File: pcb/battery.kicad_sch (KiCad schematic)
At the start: 45 parts

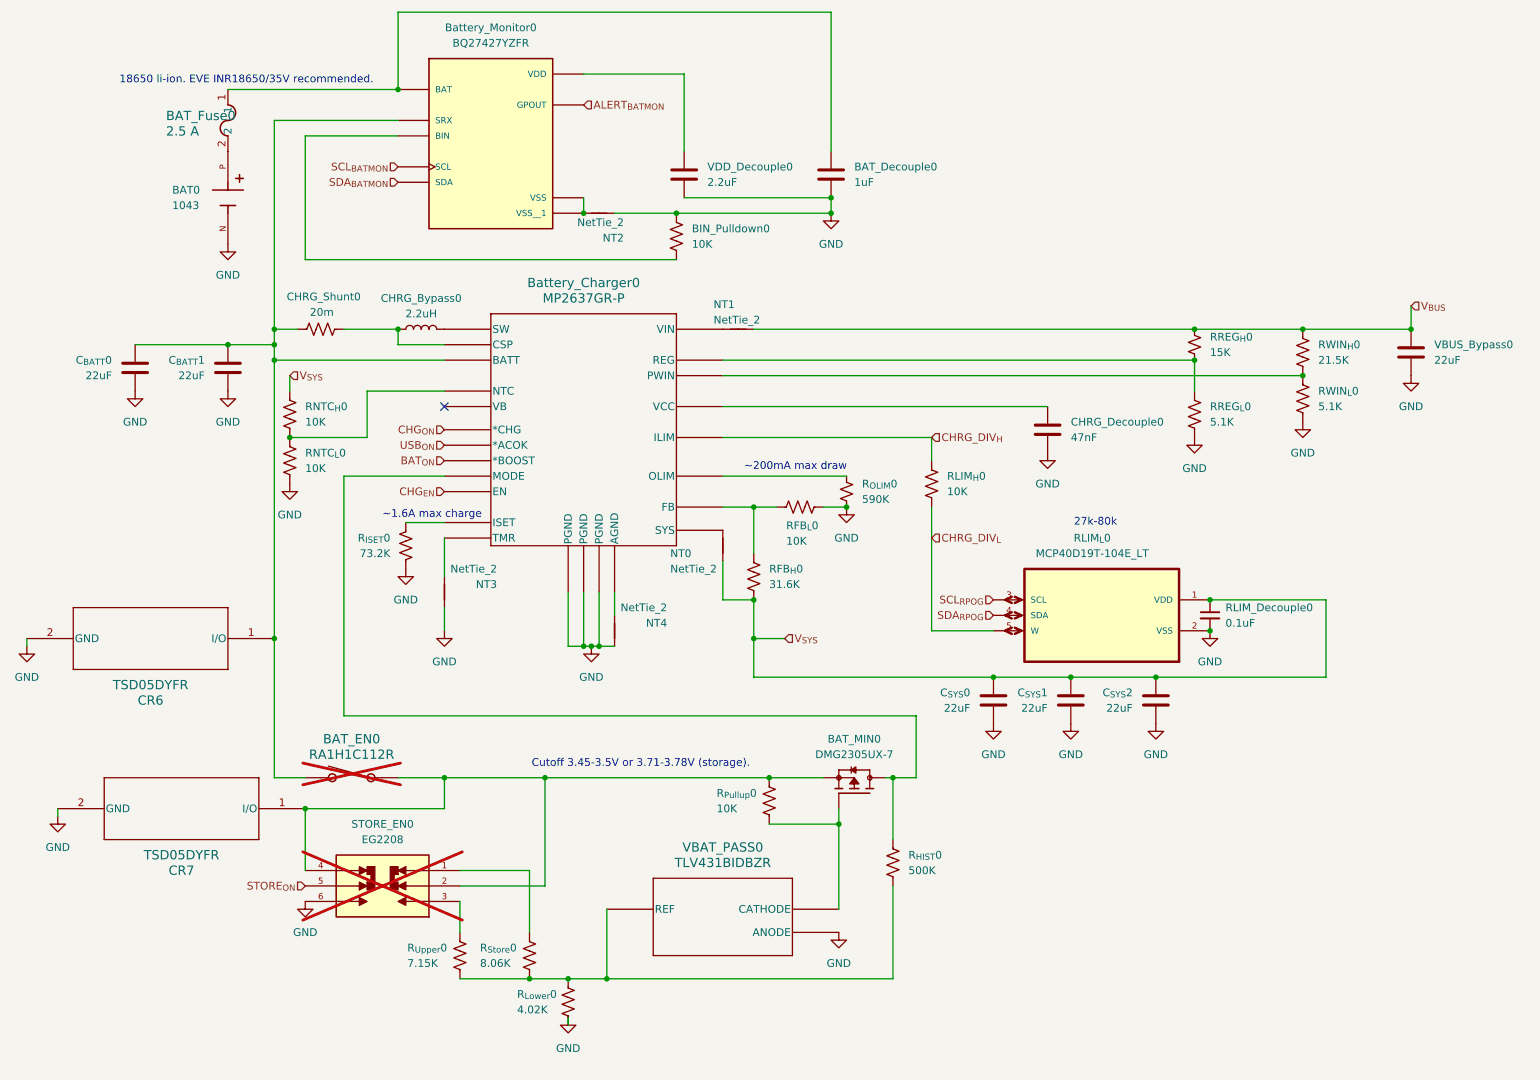
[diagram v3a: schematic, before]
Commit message: Create right hand order for JLCPCB
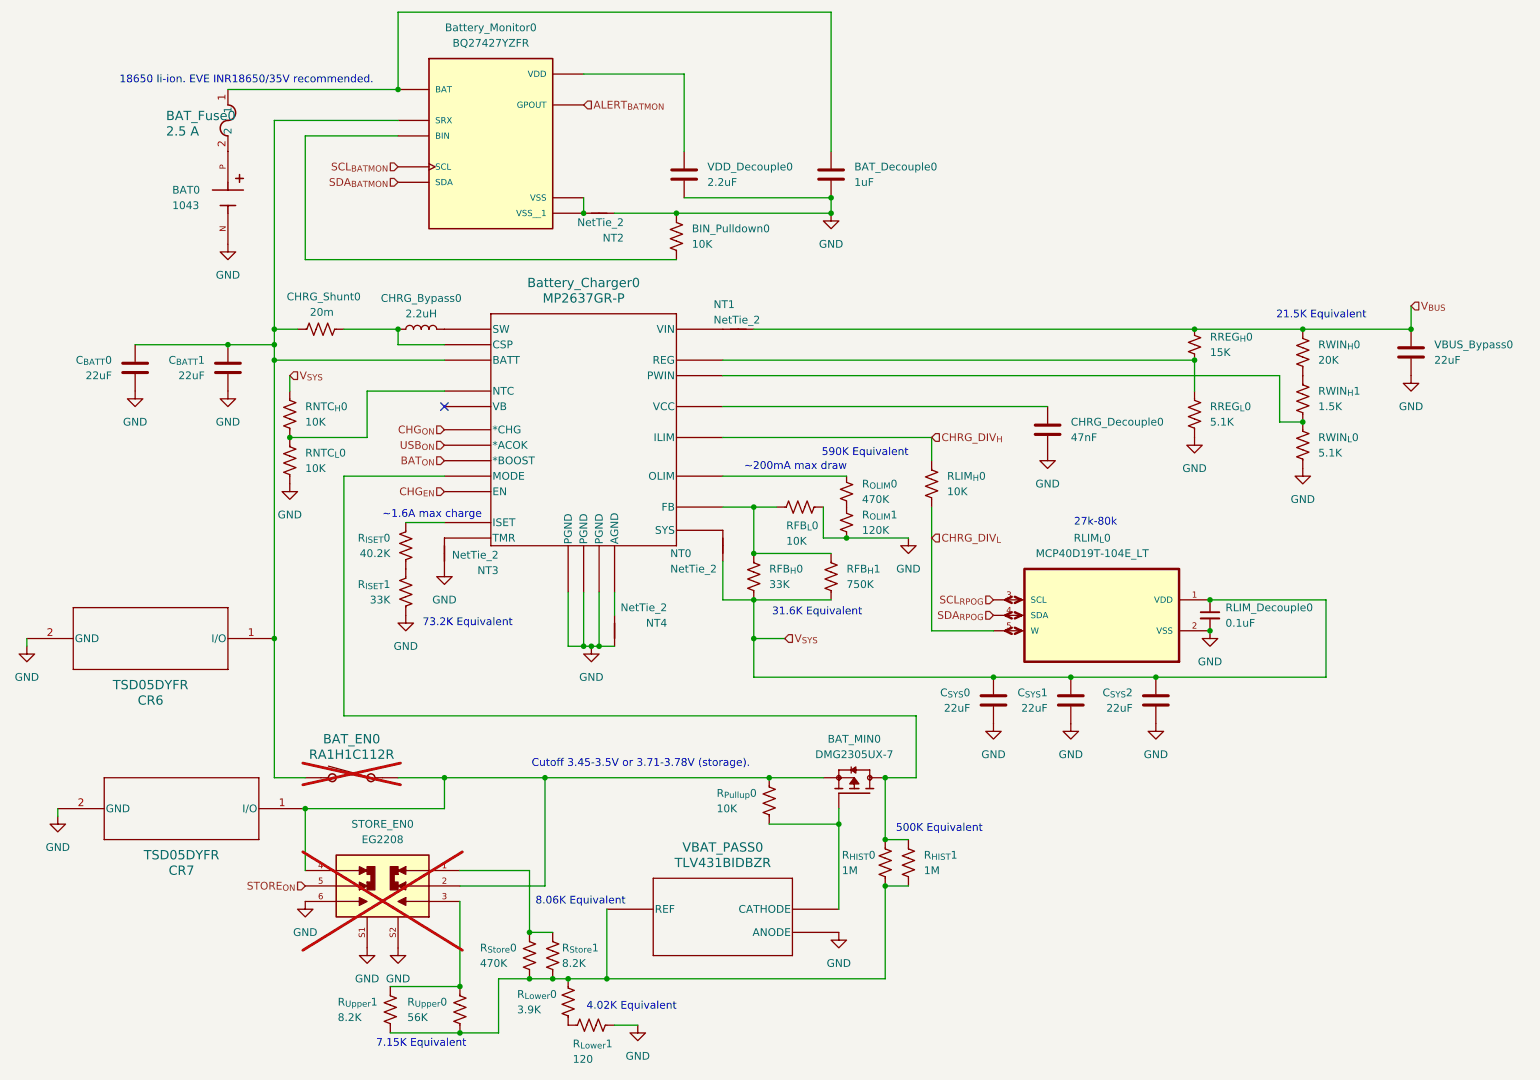
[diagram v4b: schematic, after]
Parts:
- added RFB_{H}1: 750K, Resistor_SMD:R_0603_1608Metric, symbol Device:R_US
- added RWIN_{H}1: 1.5K, Resistor_SMD:R_0402_1005Metric, symbol Device:R_US
- added R_{HIST}1: 1M, Resistor_SMD:R_0402_1005Metric, symbol Device:R_US
- added R_{ISET}1: 33K, Resistor_SMD:R_0603_1608Metric, symbol Device:R_US
- added R_{Lower}1: 120, Resistor_SMD:R_0603_1608Metric, symbol Device:R_US
- added R_{OLIM}1: 120K, Resistor_SMD:R_0402_1005Metric, symbol Device:R_Small_US
- added R_{Store}1, R_{Upper}1: 8.2K, Resistor_SMD:R_0402_1005Metric, symbol Device:R_US
- BAT_Decouple0: LCSC C2823 -> C28323
- CHRG_Bypass0: footprint Inductor_SMD:L_1210_3225Metric -> Inductor_SMD:L_0805_2012Metric; LCSC C70960 -> C1043
- C_{BATT}0, C_{BATT}1, C_{SYS}0, C_{SYS}1, C_{SYS}2, VBUS_Bypass0: LCSC C12891 -> C5672
- RFB_{H}0: value 31.6K -> 33K; footprint Resistor_SMD:R_0805_2012Metric -> Resistor_SMD:R_0603_1608Metric; LCSC C17623 -> C4216
- RWIN_{H}0: value 21.5K -> 20K; footprint Resistor_SMD:R_0805_2012Metric -> Resistor_SMD:R_0402_1005Metric; LCSC C17545 -> C25765
- R_{HIST}0: value 500K -> 1M; footprint Resistor_SMD:R_0805_2012Metric -> Resistor_SMD:R_0402_1005Metric; LCSC C3097783 -> C26083
- R_{ISET}0: value 73.2K -> 40.2K; footprint Resistor_SMD:R_0805_2012Metric -> Resistor_SMD:R_0603_1608Metric; LCSC C17814 -> C12447
- R_{Lower}0: value 4.02K -> 3.9K; footprint Resistor_SMD:R_0805_2012Metric -> Resistor_SMD:R_0603_1608Metric; LCSC C17663 -> C23018
- R_{OLIM}0: value 590K -> 470K; footprint Resistor_SMD:R_0805_2012Metric -> Resistor_SMD:R_0402_1005Metric; LCSC C17762 -> C25790
- R_{Store}0: value 8.06K -> 470K; footprint Resistor_SMD:R_0805_2012Metric -> Resistor_SMD:R_0402_1005Metric; LCSC C19006 -> C25790
- R_{Upper}0: value 7.15K -> 56K; footprint Resistor_SMD:R_0805_2012Metric -> Resistor_SMD:R_0402_1005Metric; LCSC C17806 -> C25796
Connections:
- net GND: now also STORE_EN0.S1, STORE_EN0.S2, R_{ISET}1.2, R_{Lower}1.2, R_{OLIM}1.2; no longer R_{ISET}0.2, R_{Lower}0.2, R_{OLIM}0.2
- net V_{SYS}: now also RFB_{H}1.2
- net at R_{HIST}0.2, R_{Lower}0.1, R_{Store}0.2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: now also R_{HIST}1.2, R_{Store}1.2, R_{Upper}1.2
- net at BAT_MIN0.3, Battery_Charger0.19 (MODE), R_{HIST}0.1: now also R_{HIST}1.1
- net at Battery_Charger0.14 (PWIN), RWIN_{L}0.1: now also RWIN_{H}1.2; no longer RWIN_{H}0.2
- net at Battery_Charger0.10 (FB), RFB_{H}0.1, RFB_{L}0.2: now also RFB_{H}1.1
- net at R_{Upper}0.1, STORE_EN0.3: now also R_{Upper}1.1
- net at R_{Store}0.1, STORE_EN0.1: now also R_{Store}1.1
- new net: R_{Lower}0.2, R_{Lower}1.1
- new net: R_{ISET}0.2, R_{ISET}1.1
- new net: RWIN_{H}0.2, RWIN_{H}1.1
- new net: R_{OLIM}0.2, R_{OLIM}1.1
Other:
- note added: "21.5K Equivalent"
- note added: "31.6K Equivalent"
- note added: "4.02K Equivalent"
- note added: "500K Equivalent"
- note added: "590K Equivalent"
- note added: "7.15K Equivalent"
- note added: "73.2K Equivalent"
- note added: "8.06K Equivalent"
- moved on the sheet: NT3, RWIN_{L}0, R_{HIST}0, R_{Upper}0

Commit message: Various debug tweaks
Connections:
- net at BAT_EN0.1, BAT_MIN0.2, CR7.1 (I/O)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: no longer STORE_EN0.4
- no-connect marks 1 -> 2
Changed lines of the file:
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@@
-	)
-	(junction
-		(at 68.58 154.94)
-		(diameter 0)
-		(color 0 0 0 0)
 	)
 	(junction
@@
 		(diameter 0)
 		(color 0 0 0 0)
+	)
+	(no_connect
+		(at 68.58 165.1)
 	)
 	(no_connect
@@
 		)
 		(stroke
-			(width 0)
-			(type default)
-		)
-	)
-	(wire
-		(pts
-			(xy 68.58 165.1) (xy 68.58 154.94)
-		)
-		(stroke
